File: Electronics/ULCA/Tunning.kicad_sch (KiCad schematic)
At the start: 12 parts, among them U3 ${SIM.PARAMS}, U4 ${SIM.PARAMS}

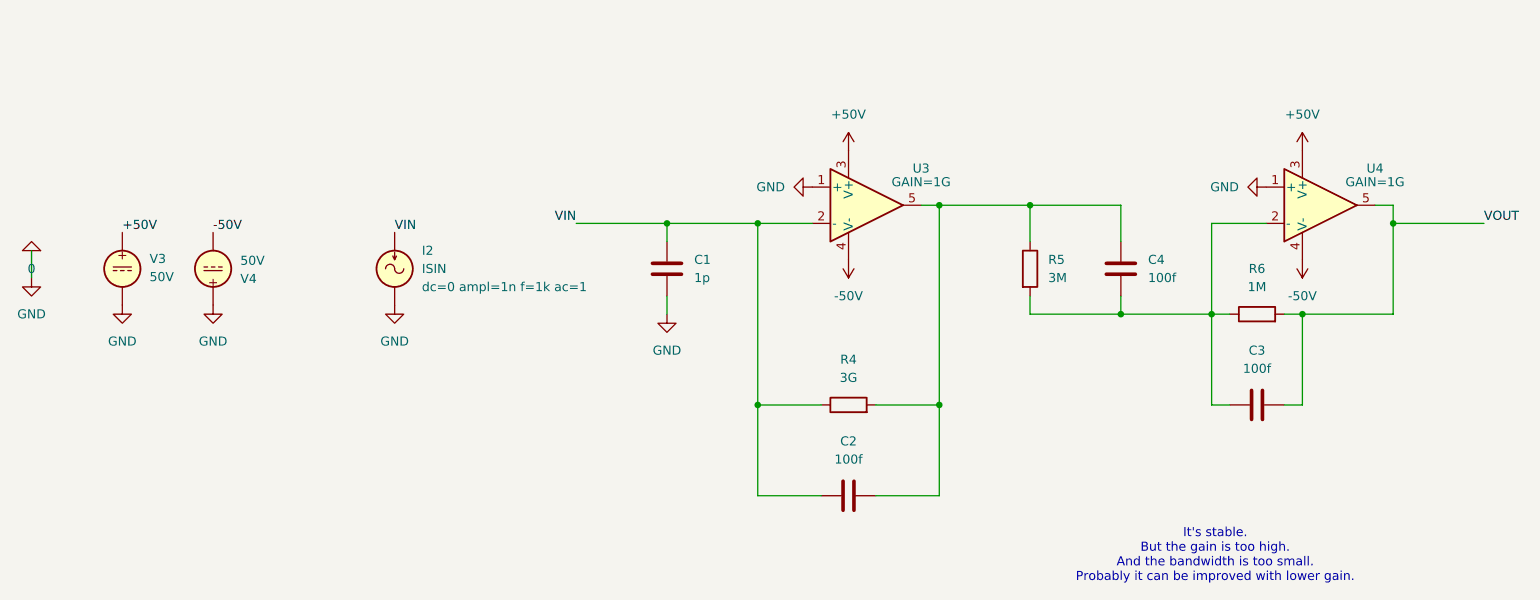
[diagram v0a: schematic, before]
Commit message: Achieve good specifications under unrealistic conditions for the ULCA
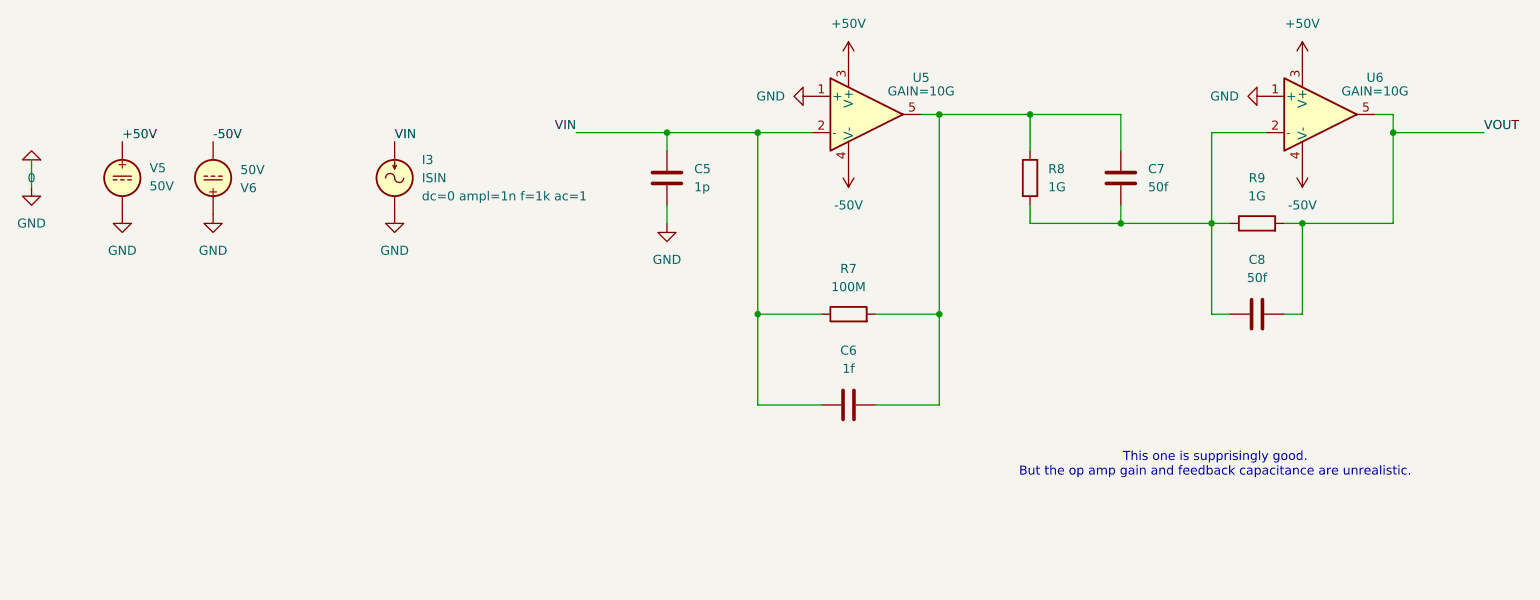
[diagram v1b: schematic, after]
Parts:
- removed C1: 1p, symbol Device:C
- removed C2, C3, C4: 100f, symbol Device:C
- removed I2: ISIN, symbol Simulation_SPICE:ISIN
- removed R4: 3G, symbol Device:R
- removed R5: 3M, symbol Device:R
- removed R6: 1M, symbol Device:R
- removed U3, U4: ${SIM.PARAMS}, symbol Simulation_SPICE:OPAMP
- removed V3, V4: 50V, symbol Simulation_SPICE:VDC
- added C5: 1p, symbol Device:C
- added C6: 1f, symbol Device:C
- added C7, C8: 50f, symbol Device:C
- added I3: ISIN, symbol Simulation_SPICE:ISIN
- added R7: 100M, symbol Device:R
- added R8, R9: 1G, symbol Device:R
- added U5, U6: ${SIM.PARAMS}, symbol Simulation_SPICE:OPAMP
- added V5, V6: 50V, symbol Simulation_SPICE:VDC
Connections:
- net +50V: now also U5.3 (V+), U6.3 (V+), V5.1
- net -50V: now also U5.4 (V-), U6.4 (V-), V6.2
- net 0: now also C5.2, I3.2, U5.1 (+), U6.1 (+), V5.2, V6.1
- net VIN: now also C5.1, C6.1, I3.1, R7.1, U5.2 (-)
- net VOUT: now also C8.2, R9.2, U6.5
- new net: C6.2, C7.2, R7.2, R8.1, U5.5
- new net: C7.1, C8.1, R8.2, R9.1, U6.2 (-)
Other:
- note added: "This one is supprisingly good. But the op amp gain and feedback capacitance are unrealistic."
- note removed: "It's stable.r But the gain is too high. And the bandwidth is too small. Probably it can be improved with lower gain."
